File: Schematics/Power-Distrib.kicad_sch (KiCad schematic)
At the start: 67 parts, among them J63 Screw_Terminal_01x02, J64 Screw_Terminal_01x02, J65 Screw_Terminal_01x02, J66 Conn_01x03, J67 Conn_01x03, J68 Conn_01x03, J69 Conn_01x03, J70 Conn_01x02, J71 Conn_01x02, J72 Conn_01x02, J73 Conn_01x02, J74 Conn_01x02, J75 Conn_01x02, J76 Conn_01x02, J77 Conn_01x02, J78 Conn_01x03, J79 Conn_01x03, J80 Conn_01x03, J81 Conn_01x03, J82 Conn_01x03, J83 Conn_01x03, J84 Conn_01x02, J85 Jack-DC, J86 Jack-DC, J87 Conn_01x03, J88 Conn_01x03, J90 Conn_01x03, J91 Conn_01x03, J92 Conn_01x03, J93 Conn_01x03, J94 Conn_01x03, K1 Relay_SPDT, U87 LM7805, U88 LM7812, U89 LM7912, U90 LM7805, U91 LM7812, U92 LM7912

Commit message: Updated schematics including VCO and VCF daughter boards
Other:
- company:       MLE Tech                  Cedar Park, TX -> (none)
- title: Synth #2 -> Power Distribution
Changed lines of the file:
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@@
 	(paper "USLegal")
 	(title_block
-		(title "Synth #2")
-		(date "2023-07-27")
-		(rev "0.1")
-		(company "      MLE Tech                  Cedar Park, TX")
-		(comment 2 "In Development")
+		(title "Power Distribution")
+		(date "2025-01-16")
+		(rev "1.8")
+		(comment 1 "In Development ")
 	)
 	(junction

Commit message: Cleaned up page advance on display controls.
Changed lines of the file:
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@@
 (kicad_sch
-	(version 20231120)
+	(version 20250114)
 	(generator "eeschema")
-	(generator_version "8.0")
+	(generator_version "9.0")
 	(paper "USLegal")
 	(title_block
@@
 		(comment 1 "In Development ")
 	)
+	(rectangle
+		(start 194.31 123.19)
+		(end 307.34 170.18)
+		(stroke
+			(width 0)
+			(type default)
+		)
+		(fill
+			(type none)
+		)
+	)
+	(rectangle
+		(start 194.31 15.24)
+		(end 331.47 72.39)
+		(stroke
+			(width 0)
+			(type default)
+		)
+		(fill
+			(type none)
+		)
+	)
+	(rectangle
+		(start 13.97 15.24)
+		(end 187.96 190.5)
+		(stroke
+			(width 0)
+			(type default)
+		)
+		(fill
+			(type none)
+		)
+	)
+	(text "Power Dist 2"
+		(exclude_from_sim no)
+		(at 247.65 16.51 0)
+		(effects
+			(font
+				(size 1.27 1.27)
+			)
+		)
+	)
+	(text "7V"
+		(exclude_from_sim no)
+		(at 33.02 43.18 0)
+		(effects
+			(font
+				(size 1.016 1.016)
+			)
+			(justify right bottom)
+		)
+	)
+	(text "+5A"
+		(exclude_from_sim no)
+		(at 124.46 82.55 0)
+		(effects
+			(font
+				(size 1.27 1.27)
+			)
+			(justify left bottom)
+		)
+	)
+	(text "12V\n3A\nWallWart"
+		(exclude_from_sim no)
+		(at 199.39 148.844 0)
+		(effects
+			(font
+				(size 1.016 1.016)
+			)
+		)
+	)
+	(text "-15V"
+		(exclude_from_sim no)
+		(at 33.02 170.8404 0)
+		(effects
+			(font
+				(size 1.016 1.016)
+			)
+			(justify right bottom)
+		)
+	)
+	(text "+5D"
+		(exclude_from_sim no)
+		(at 125.095 43.18 0)
+		(effects
+			(font
+				(size 1.27 1.27)
+			)
+			(justify left bottom)
+		)
+	)
+	(text "Power Controller 1"
+		(exclude_from_sim no)
+		(at 247.7977 124.9012 0)
+		(effects
+			(font
+				(size 1.27 1.27)
+			)
+		)
+	)
+	(text "15V"
+		(exclude_from_sim no)
+		(at 27.686 104.14 0)
+		(effects
+			(font
+				(size 1.016 1.016)
+			)
+			(justify right bottom)
+		)
+	)
+	(text "5V\nControl"
+		(exclude_from_sim no)
+		(at 199.39 162.052 0)
+		(effects
+			(font
+				(size 1.016 1.016)
+			)
+		)
+	)
+	(text "Power Dist 1"
+		(exclude_from_sim no)
+		(at 91.44 16.51 0)
+		(effects
+			(font
+				(size 1.27 1.27)
+			)
+		)
+	)
+	(text "12V\nto\nUSB Hub"
+		(exclude_from_sim no)
+		(at 302.514 145.796 0)
+		(effects
+			(font
+				(size 1.016 1.016)
+			)
+		)
+	)
 	(junction
 		(at 248.92 127)
@@
 		)
 	)
-	(rectangle
-		(start 194.31 123.19)
-		(end 307.34 170.18)
-		(stroke
-			(width 0)
-			(type default)
-		)
-		(fill
-			(type none)
-		)
-	)
-	(rectangle
-		(start 194.31 15.24)
-		(end 331.47 72.39)
-		(stroke
-			(width 0)
-			(type default)
-		)
-		(fill
-			(type none)
-		)
-	)
-	(rectangle
-		(start 13.97 15.24)
-		(end 187.96 190.5)
-		(stroke
-			(width 0)
-			(type default)
-		)
-		(fill
-			(type none)
-		)
-	)
-	(text "Power Dist 2"
-		(exclude_from_sim no)
-		(at 247.65 16.51 0)
-		(effects
-			(font
-				(size 1.27 1.27)
-			)
-		)
-	)
-	(text "7V"
-		(exclude_from_sim no)
-		(at 33.02 43.18 0)
-		(effects
-			(font
-				(size 1.016 1.016)
-			)
-			(justify right bottom)
-		)
-	)
-	(text "+5A"
-		(exclude_from_sim no)
-		(at 124.46 82.55 0)
-		(effects
-			(font
-				(size 1.27 1.27)
-			)
-			(justify left bottom)
-		)
-	)
-	(text "12V\n3A\nWallWart"
-		(exclude_from_sim no)
-		(at 199.39 148.844 0)
-		(effects
-			(font
-				(size 1.016 1.016)
-			)
-		)
-	)
-	(text "-15V"
-		(exclude_from_sim no)
-		(at 33.02 170.8404 0)
-		(effects
-			(font
-				(size 1.016 1.016)
-			)
-			(justify right bottom)
-		)
-	)
-	(text "+5D"
-		(exclude_from_sim no)
-		(at 125.095 43.18 0)
-		(effects
-			(font
-				(size 1.27 1.27)
-			)
-			(justify left bottom)
-		)
-	)
-	(text "Power Controller 1"
-		(exclude_from_sim no)
-		(at 247.7977 124.9012 0)
-		(effects
-			(font
-				(size 1.27 1.27)
-			)
-		)
-	)
-	(text "15V"
-		(exclude_from_sim no)
-		(at 27.686 104.14 0)
-		(effects
-			(font
-				(size 1.016 1.016)
-			)
-			(justify right bottom)
-		)
-	)
-	(text "5V\nControl"
-		(exclude_from_sim no)
-		(at 199.39 162.052 0)
-		(effects
-			(font
-				(size 1.016 1.016)
-			)
-		)
-	)
-	(text "Power Dist 1"
-		(exclude_from_sim no)
-		(at 91.44 16.51 0)
-		(effects
-			(font
-				(size 1.27 1.27)
-			)
-		)
-	)
-	(text "12V\nto\nUSB Hub"
-		(exclude_from_sim no)
-		(at 302.514 145.796 0)
-		(effects
-			(font
-				(size 1.016 1.016)
-			)
-		)
-	)
 	(label "+7D"
 		(at 124.46 22.86 0)
-		(fields_autoplaced yes)
 		(effects
 			(font
@@
 	(label "+12A"
 		(at 129.5386 104.14 180)
-		(fields_autoplaced yes)
 		(effects
 			(font
@@
 	(label "-12A"
 		(at 124.4971 170.18 0)
-		(fields_autoplaced yes)
 		(effects
 			(font

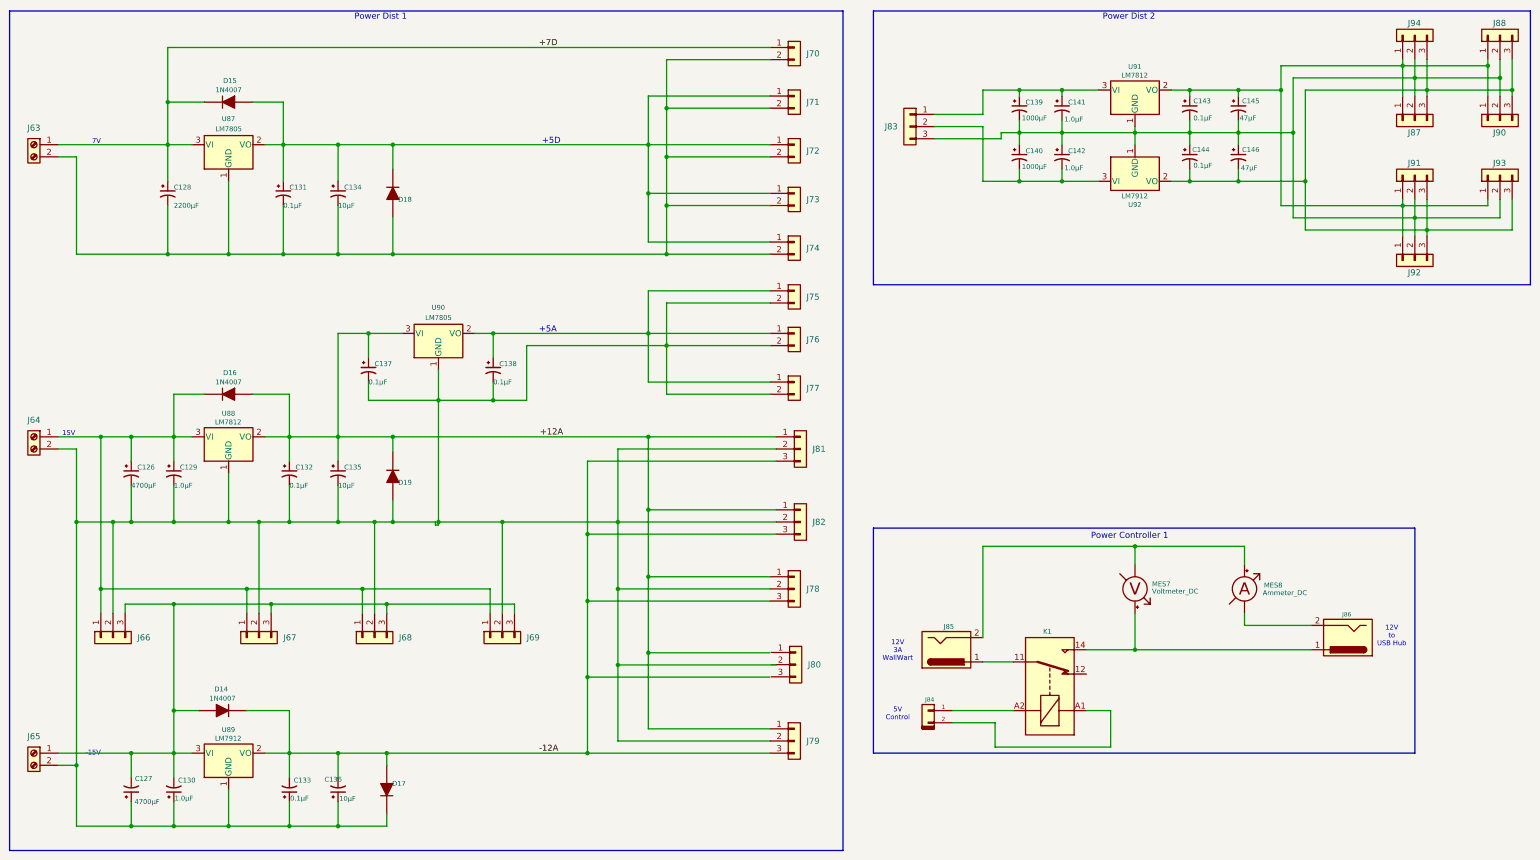
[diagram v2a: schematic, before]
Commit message: Fixed bugs in voice selection on configuration.  Reorganized schematics to have different master drawings for power and audio paths.  Started work on dual 3-pole state variable filter with resonance.
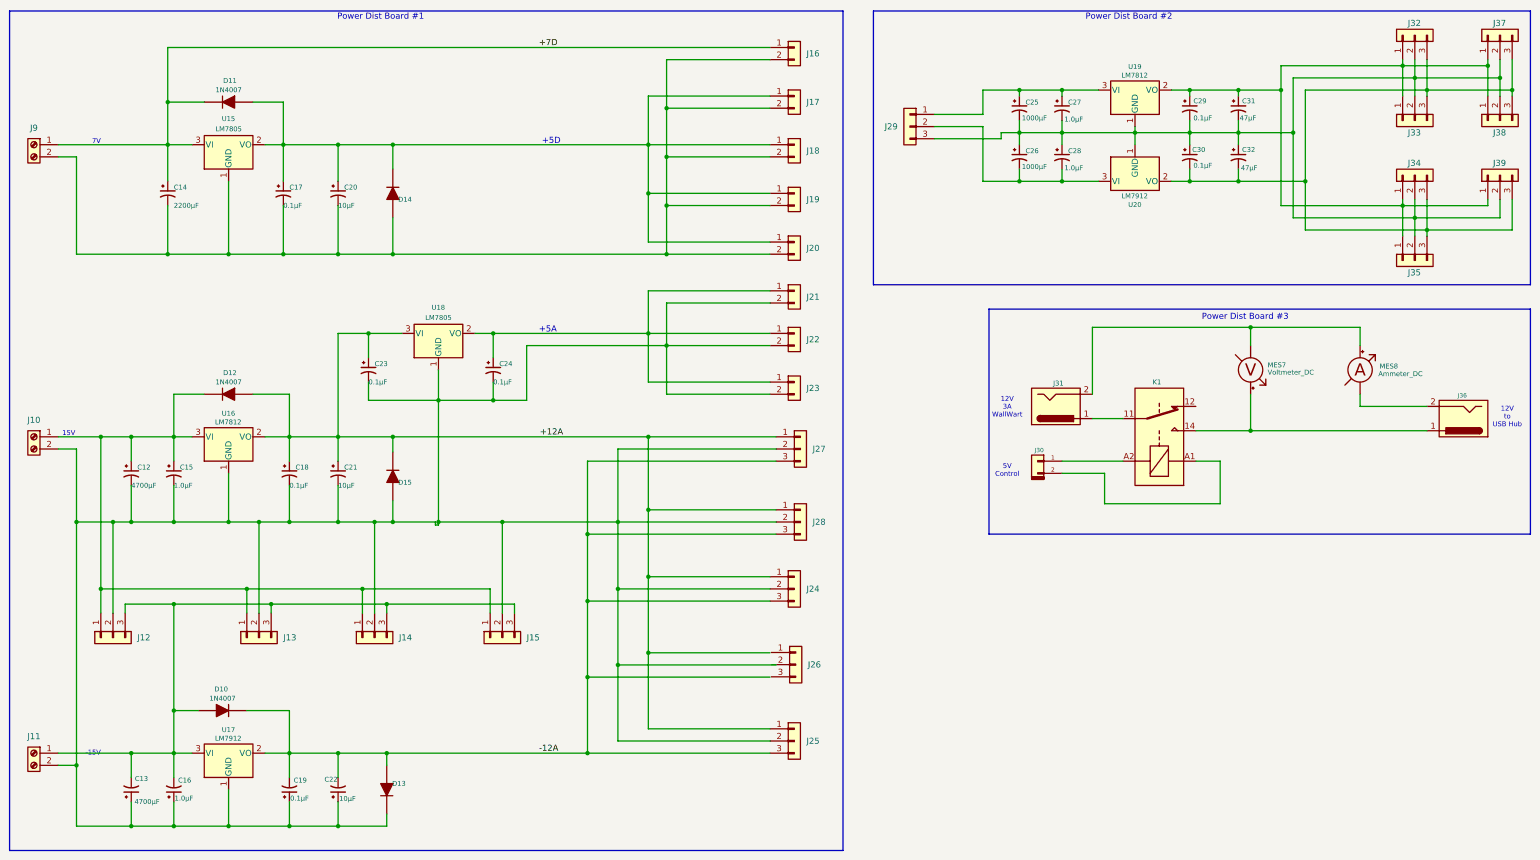
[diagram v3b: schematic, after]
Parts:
- renumbered C126 to C12, C127 to C13, C128 to C14, C129 to C15, C130 to C16, C131 to C17, C132 to C18, C133 to C19, C134 to C20, C135 to C21, C136 to C22, C137 to C23, C138 to C24, C139 to C25, C140 to C26, C141 to C27, C142 to C28, C143 to C29, C144 to C30, C145 to C31, C146 to C32, D14 to D10, D15 to D11, D16 to D12, D17 to D13, D18 to D14, D19 to D15, J64 to J10, J65 to J11, J66 to J12, J67 to J13, J68 to J14, J69 to J15, J70 to J16, J71 to J17, J72 to J18, J73 to J19, J74 to J20, J75 to J21, J76 to J22, J77 to J23, J78 to J24, J79 to J25, J80 to J26, J81 to J27, J82 to J28, J83 to J29, J84 to J30, J85 to J31, J94 to J32, J87 to J33, J91 to J34, J92 to J35, J86 to J36, J88 to J37, J90 to J38, J93 to J39, J63 to J9, U87 to U15, U88 to U16, U89 to U17, U90 to U18, U91 to U19, U92 to U20
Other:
- note added: "Power Dist Board #1"
- note added: "Power Dist Board #2"
- note added: "Power Dist Board #3"
- note removed: "Power Controller 1"
- note removed: "Power Dist 1"
- note removed: "Power Dist 2"
- moved on the sheet: J30, J31, J36, K1, MES7, MES8
